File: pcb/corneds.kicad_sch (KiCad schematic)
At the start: 120 parts, among them J3 AudioJack4, J4 AudioJack4, SW1 SW_Push, SW10 SW_Push, SW11 SW_Push, SW12 SW_Push, SW13 SW_Push, SW14 SW_Push, SW15 SW_Push, SW16 SW_Push, SW17 SW_Push, SW18 SW_Push, SW19 SW_Push, SW2 SW_Push, SW20 SW_Push, SW21 SW_Push, SW22 SW_Push, SW23 SW_Push, SW24 SW_Push, SW25 SW_Push, SW26 SW_Push, SW27 SW_Push, SW28 SW_Push, SW29 SW_Push, SW3 SW_Push, SW30 SW_Push, SW31 SW_Push, SW32 SW_Push, SW33 SW_Push, SW34 SW_Push, SW35 SW_Push, SW36 SW_Push, SW37 SW_Push, SW38 SW_Push, SW39 SW_Push, SW4 SW_Push, SW40 SW_Push, SW41 SW_Push, SW42 SW_Push, SW5 SW_Push, SW6 SW_Push, SW7 SW_Push, SW8 SW_Push, SW9 SW_Push, U1 Pico, U2 Pico, U3 SWD_Connector_3pin, U4 SWD_Connector_3pin, U5 Debug_UART_l, U6 Debug_UART_r

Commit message: routed left side, placed 3 more mounting holes but want one more
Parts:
- J3, J4: footprint Connector_Audio:Jack_3.5mm_PJ320E_Horizontal -> entropy:Jack_3.5mm_boardsource_TRRS_TH
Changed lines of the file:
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@@
       (effects (font (size 1.27 1.27)))
     )
-    (property "Footprint" "Connector_Audio:Jack_3.5mm_PJ320E_Horizontal" (at 220.98 130.81 0)
+    (property "Footprint" "entropy:Jack_3.5mm_boardsource_TRRS_TH" (at 220.98 130.81 0)
       (effects (font (size 1.27 1.27)) hide)
     )
@@
       (effects (font (size 1.27 1.27)))
     )
-    (property "Footprint" "Connector_Audio:Jack_3.5mm_PJ320E_Horizontal" (at 220.98 63.5 0)
-      (effects (font (size 1.27 1.27)) hide)
-    )
+    (property "Footprint" "entropy:Jack_3.5mm_boardsource_TRRS_TH" (at 220.98 63.5 0)
+      (effects (font (size 1.27 1.27)) hide)
+    )

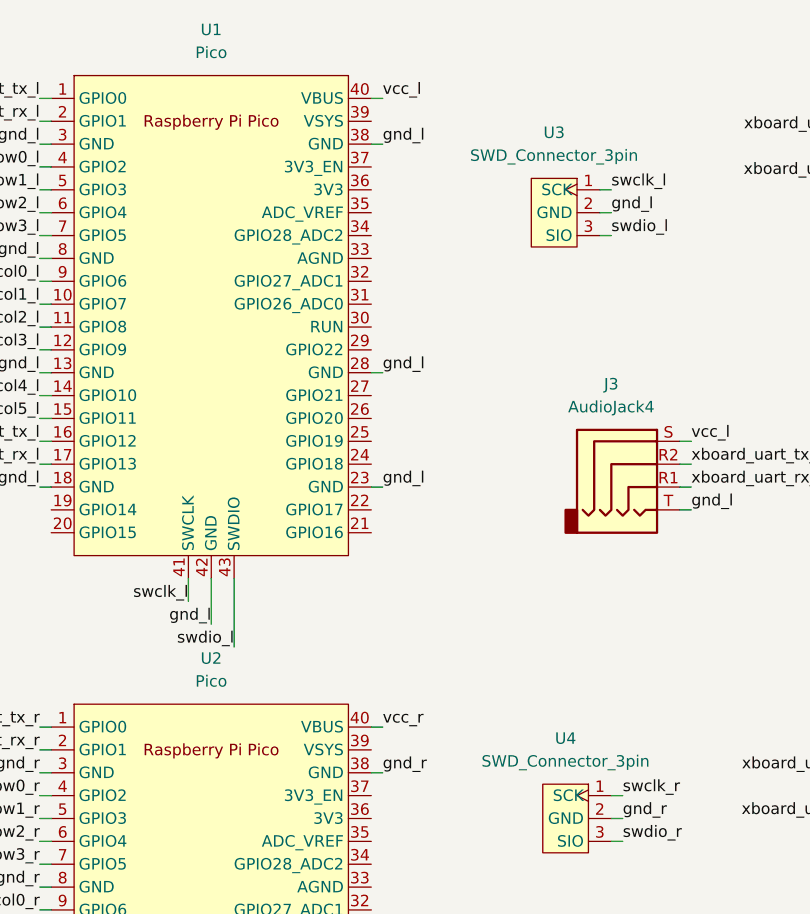
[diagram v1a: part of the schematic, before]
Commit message: made led utils to have better readability over led states and switched board power to VSYS so we can differentiate right from left based on VBUS. This will run the peripheral board at 4.8V instead of 5V due to going through two schottky diodes
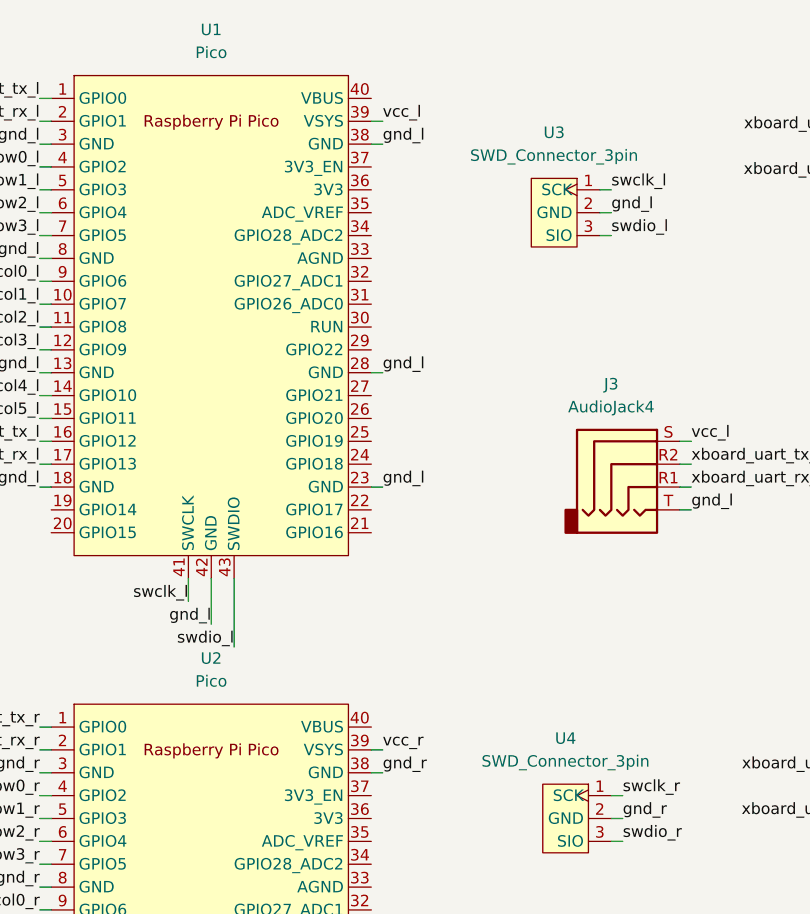
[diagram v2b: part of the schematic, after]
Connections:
- net vcc_l: now also U1.39 (VSYS); no longer U1.40 (VBUS)
- net vcc_r: now also U2.39 (VSYS); no longer U2.40 (VBUS)
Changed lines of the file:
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@@
+    (stroke (width 0) (type default))
+  )
+  (wire (pts (xy 191.77 25.4) (xy 193.04 25.4))
     (stroke (width 0) (type default))
   )
@@
     (stroke (width 0) (type default))
   )
-  (wire (pts (xy 191.77 92.71) (xy 193.04 92.71))
-    (stroke (width 0) (type default))
-  )
   (wire (pts (xy 191.77 135.89) (xy 193.04 135.89))
     (stroke (width 0) (type default))
@@
     (stroke (width 0) (type default))
   )
-  (wire (pts (xy 191.77 22.86) (xy 193.04 22.86))
-    (stroke (width 0) (type default))
-  )
   (wire (pts (xy 173.99 76.2) (xy 173.99 81.28))
     (stroke (width 0) (type default))
@@
     (stroke (width 0) (type default))
   )
+  (wire (pts (xy 191.77 95.25) (xy 193.04 95.25))
+    (stroke (width 0) (type default))
+  )
   (wire (pts (xy 38.1 38.1) (xy 38.1 50.8))
     (stroke (width 0) (type default))
@@
     (effects (font (size 1.27 1.27)) (justify right bottom))
   )
-  (label "vcc_l" (at 193.04 22.86 0) (fields_autoplaced)
+  (label "vcc_l" (at 193.04 25.4 0) (fields_autoplaced)
     (effects (font (size 1.27 1.27)) (justify left bottom))
   )
@@
     (effects (font (size 1.27 1.27)) (justify right bottom))
   )
-  (label "vcc_r" (at 193.04 92.71 0) (fields_autoplaced)
-    (effects (font (size 1.27 1.27)) (justify left bottom))
-  )
+  (label "vcc_r" (at 193.04 95.25 0) (fields_autoplaced)
+    (effects (font (size 1.27 1.27)) (justify left bottom))
+  )

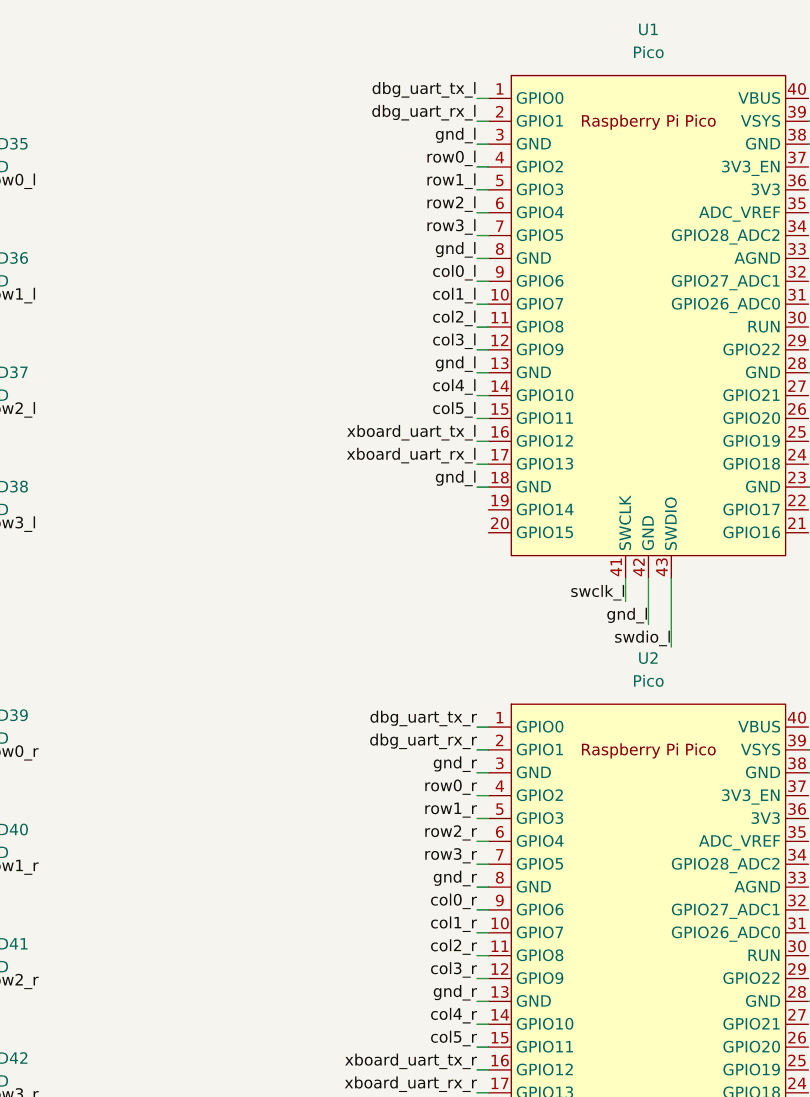
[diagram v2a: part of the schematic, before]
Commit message: dbg_uart and xboard_uart were both uart0 so I swapped dbg_uart with cols 0 and 1
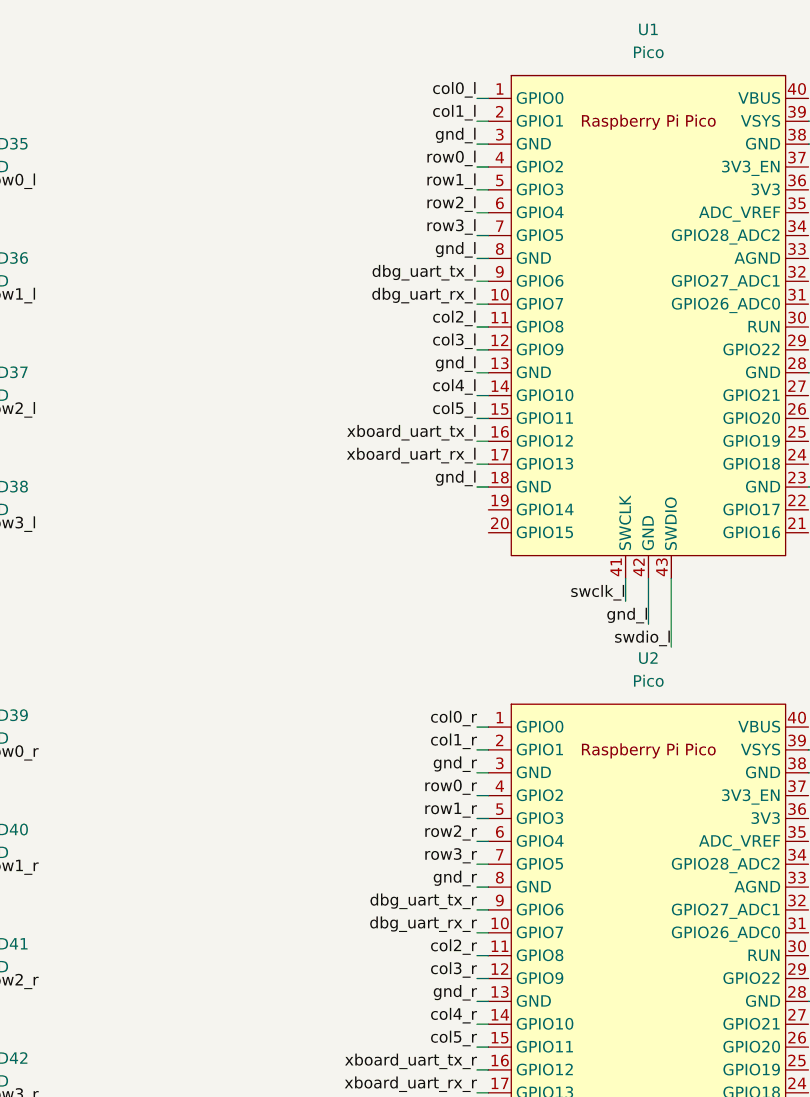
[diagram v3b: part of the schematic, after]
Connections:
- net col0_l: now also U1.1 (GPIO0); no longer U1.9 (GPIO6)
- net col0_r: now also U2.1 (GPIO0); no longer U2.9 (GPIO6)
- net col1_l: now also U1.2 (GPIO1); no longer U1.10 (GPIO7)
- net col1_r: now also U2.2 (GPIO1); no longer U2.10 (GPIO7)
- net dbg_uart_rx_l: now also U1.10 (GPIO7); no longer U1.2 (GPIO1)
- net dbg_uart_rx_r: now also U2.10 (GPIO7); no longer U2.2 (GPIO1)
- net dbg_uart_tx_l: now also U1.9 (GPIO6); no longer U1.1 (GPIO0)
- net dbg_uart_tx_r: now also U2.9 (GPIO6); no longer U2.1 (GPIO0)

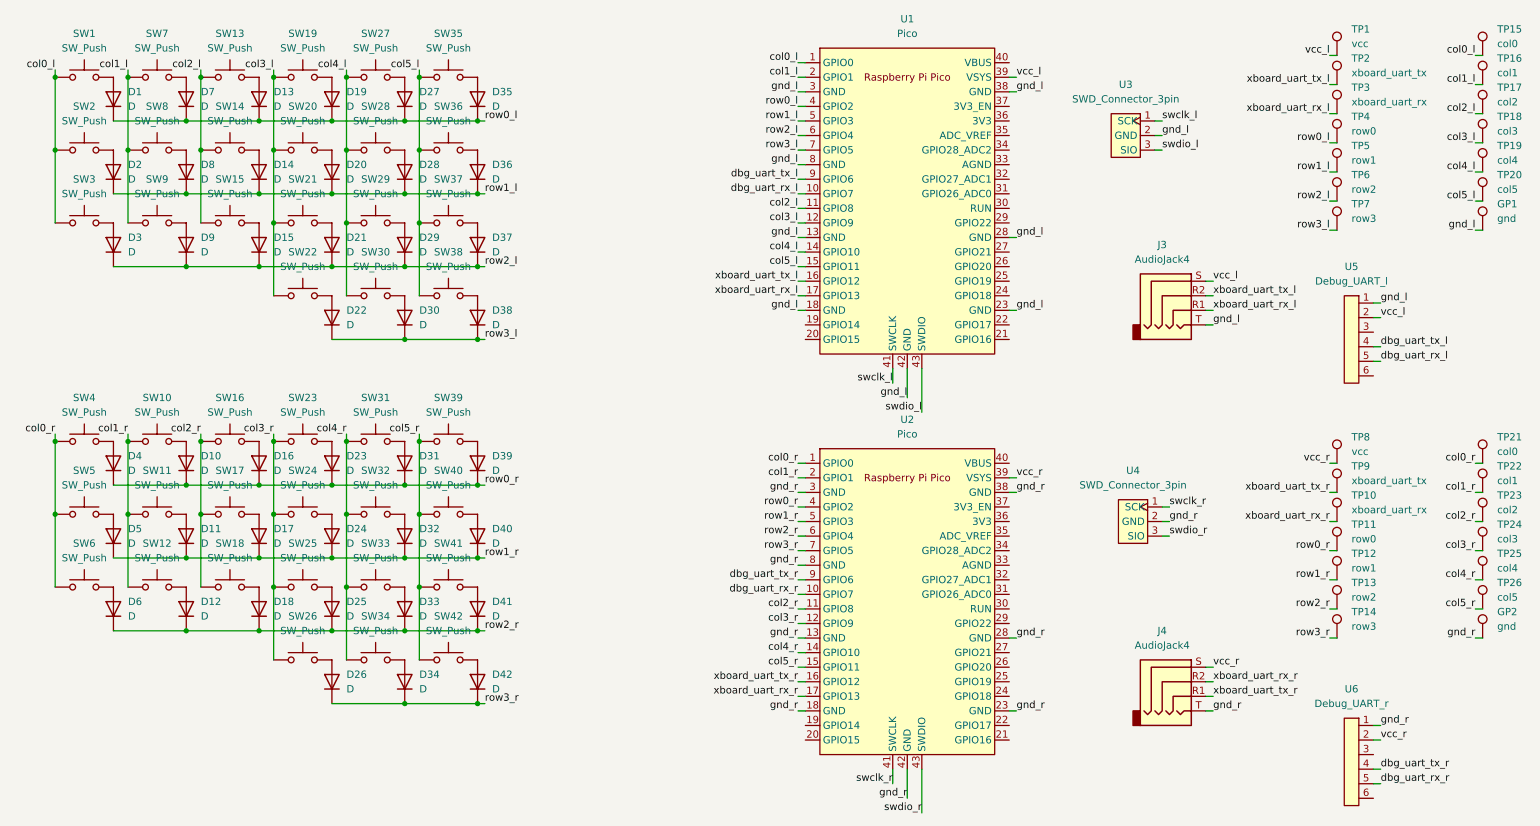
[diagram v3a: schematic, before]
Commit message: updated to rev3 of the pcb
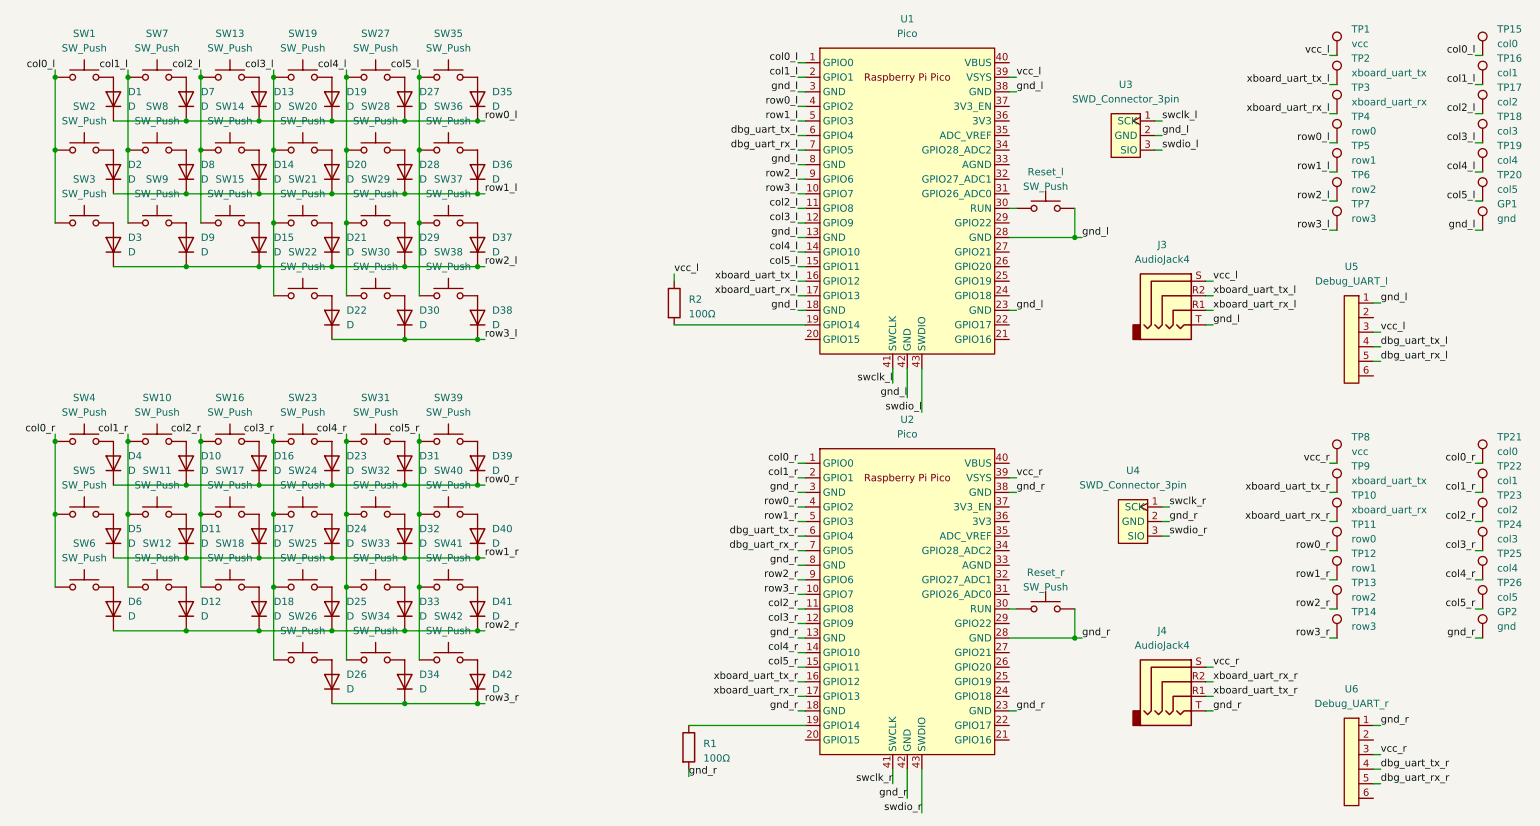
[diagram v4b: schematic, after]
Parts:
- added R1, R2: 100Ω, Resistor_SMD:R_0603_1608Metric, symbol Device:R
- added Reset_l, Reset_r: SW_Push, entropy:SW_PTS636_SK25F_SMTR, symbol Switch:SW_Push
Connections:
- net dbg_uart_rx_l: now also U1.7 (GPIO5); no longer U1.10 (GPIO7)
- net dbg_uart_rx_r: now also U2.7 (GPIO5); no longer U2.10 (GPIO7)
- net dbg_uart_tx_l: now also U1.6 (GPIO4); no longer U1.9 (GPIO6)
- net dbg_uart_tx_r: now also U2.6 (GPIO4); no longer U2.9 (GPIO6)
- net gnd_l: now also Reset_l.2
- net gnd_r: now also R1.2, Reset_r.2
- net row2_l: now also U1.9 (GPIO6); no longer U1.6 (GPIO4)
- net row2_r: now also U2.9 (GPIO6); no longer U2.6 (GPIO4)
- net row3_l: now also U1.10 (GPIO7); no longer U1.7 (GPIO5)
- net row3_r: now also U2.10 (GPIO7); no longer U2.7 (GPIO5)
- net vcc_l: now also U5.3, R2.1; no longer U5.2
- net vcc_r: now also U6.3; no longer U6.2
- net at U1.19 (GPIO14): now also R2.2
- net at U1.30 (RUN): now also Reset_l.1
- net at U2.19 (GPIO14): now also R1.1
- net at U2.30 (RUN): now also Reset_r.1

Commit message: right side is working but left side needs pins updated
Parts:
- renumbered Reset_l to Reset_l1, Reset_r to Reset_r1
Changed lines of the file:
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@@
   (symbol (lib_id "Switch:SW_Push") (at 198.12 48.26 0) (unit 1)
     (in_bom yes) (on_board yes) (dnp no) (fields_autoplaced)
-    (property "Reference" "Reset_l" (at 198.12 41.91 0)
+    (property "Reference" "Reset_l1" (at 198.12 41.91 0)
       (effects (font (size 1.27 1.27)))
     )
@@
       (project "corneds"
         (path "/359cbf27-bc01-416d-84f1-38e86191a367"
-          (reference "Reset_l") (unit 1)
+          (reference "Reset_l1") (unit 1)
         )
       )
@@
   (symbol (lib_id "Switch:SW_Push") (at 198.12 118.11 0) (unit 1)
     (in_bom yes) (on_board yes) (dnp no) (fields_autoplaced)
-    (property "Reference" "Reset_r" (at 198.12 111.76 0)
+    (property "Reference" "Reset_r1" (at 198.12 111.76 0)
       (effects (font (size 1.27 1.27)))
     )
@@
       (project "corneds"
         (path "/359cbf27-bc01-416d-84f1-38e86191a367"
-          (reference "Reset_r") (unit 1)
-        )
-      )
+          (reference "Reset_r1") (unit 1)
+        )
+      )
